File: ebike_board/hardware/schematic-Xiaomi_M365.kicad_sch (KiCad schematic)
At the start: 7 parts, among them J1 Connector_2, J3 Connector_1, U1 ESP32-S3-DevKitC

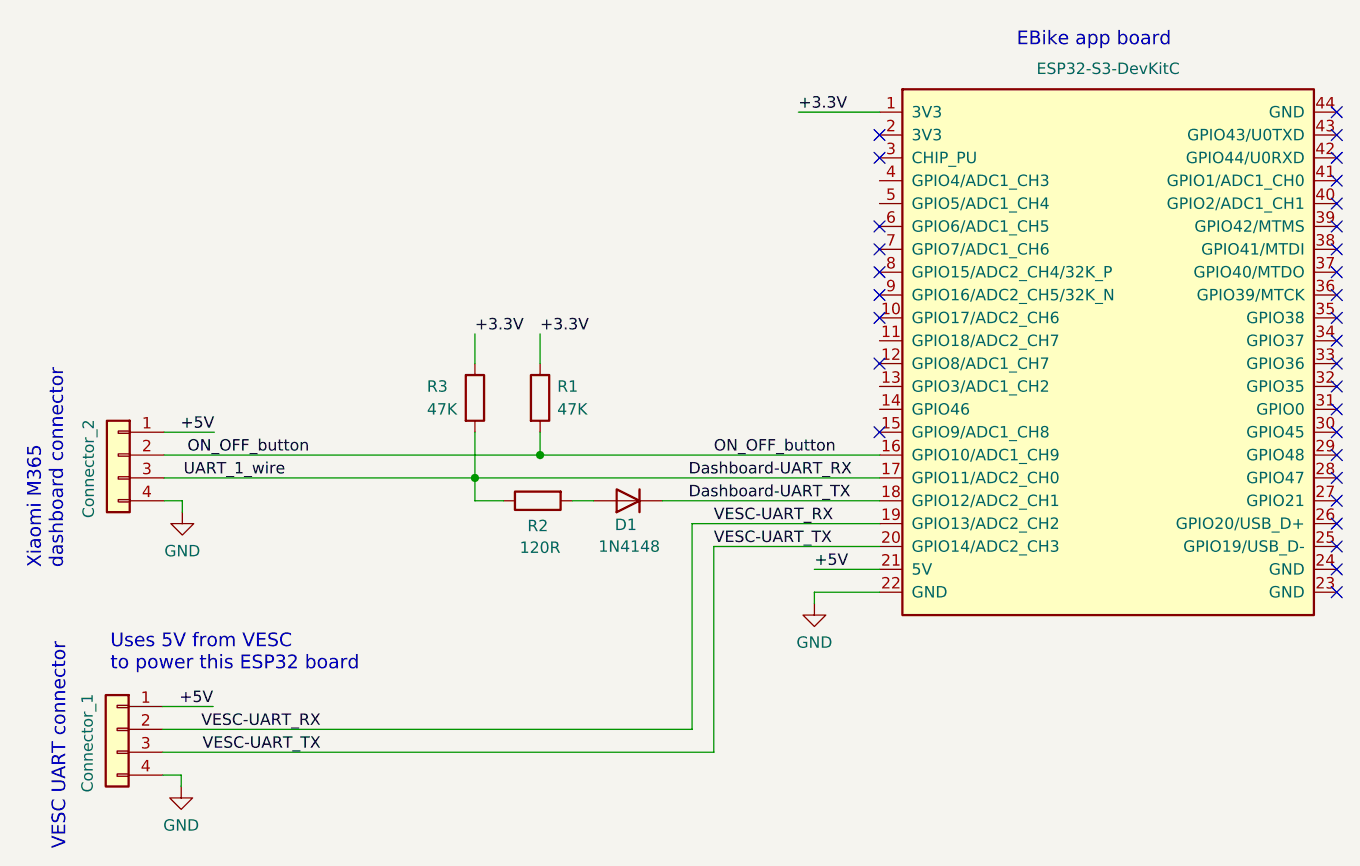
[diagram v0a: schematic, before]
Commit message: Updated schematic with tested rear light control. Rear light control works and blinks when brakes are pressed
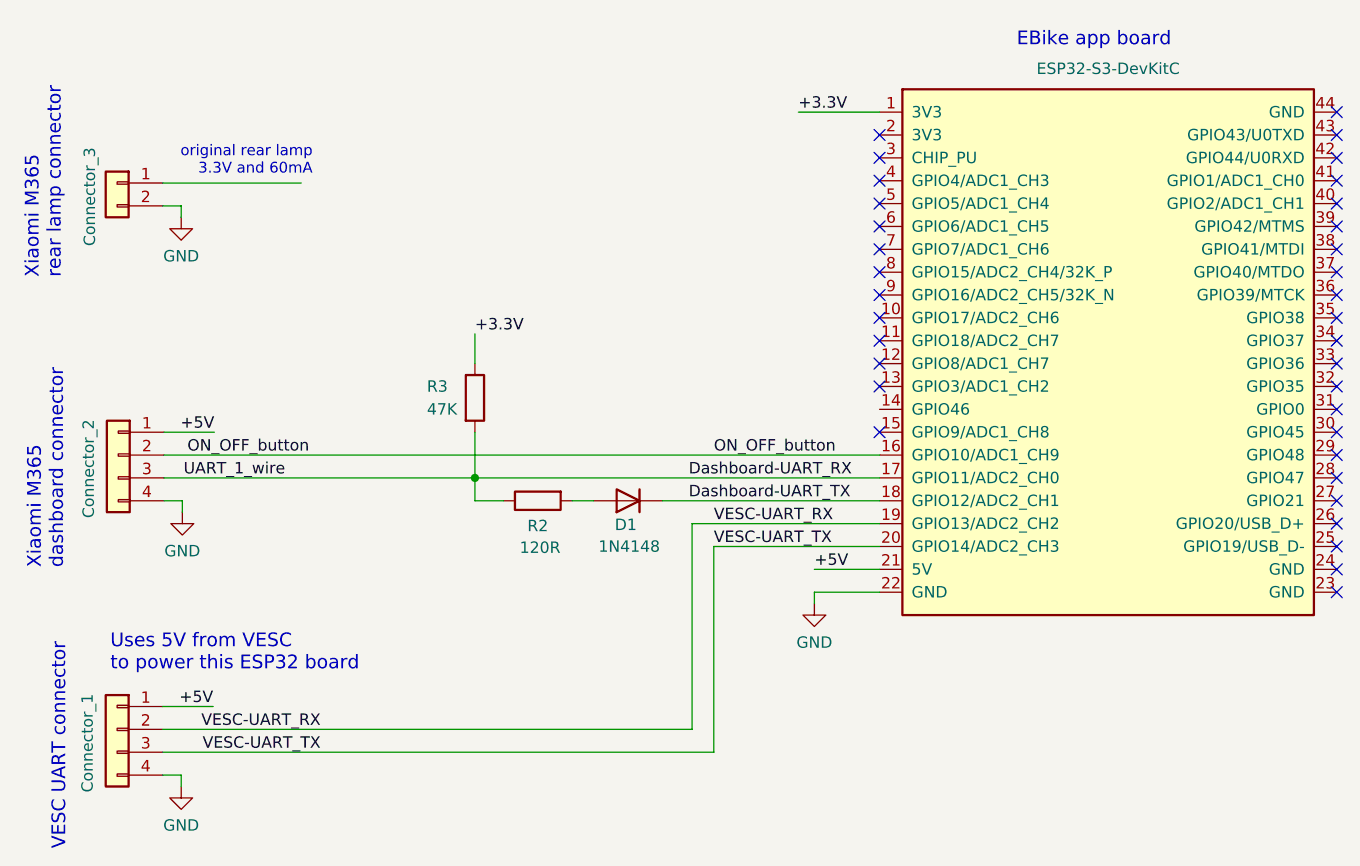
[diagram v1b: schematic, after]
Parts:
- removed R1: 47K, symbol Device:R
- added Connector_3: ~, symbol Connector_Generic:Conn_01x02
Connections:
- net GND: now also Connector_3.2 (Pin_2)
- no-connect marks 31 -> 35
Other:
- note added: "Xiaomi M365 rear lamp connector"
- note added: "original rear lamp 3.3V and 60mA"
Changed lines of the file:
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@@
   (junction (at 153.162 143.637) (diameter 0) (color 0 0 0 0)
   )
-  (junction (at 160.401 141.097) (diameter 0) (color 0 0 0 0)
-  )
+  (no_connect (at 198.12 133.477))
+  (no_connect (at 198.12 113.157))
   (no_connect (at 198.12 115.697))
   (no_connect (at 198.12 138.557))
+  (no_connect (at 198.12 128.397))
   (no_connect (at 248.92 113.157))
   (no_connect (at 198.12 105.537))
@@
   (no_connect (at 248.92 120.777))
   (no_connect (at 198.12 118.237))
-  (wire (pts (xy 160.401 130.937) (xy 160.401 127.635))
-    (stroke (width 0) (type default) (color 204 102 0 1))
-  )
+  (no_connect (at 198.12 110.617))
   (wire (pts (xy 153.162 138.557) (xy 153.162 143.637))
     (stroke (width 0) (type default))
   )
-  (wire (pts (xy 160.401 138.557) (xy 160.401 141.097))
+  (wire (pts (xy 118.491 110.871) (xy 133.858 110.871))
     (stroke (width 0) (type default))
   )
@@
   )
   (wire (pts (xy 173.99 146.177) (xy 198.12 146.177))
-    (stroke (width 0) (type default))
-  )
-  (wire (pts (xy 160.401 141.097) (xy 198.12 141.097))
     (stroke (width 0) (type default))
   )
@@
     (stroke (width 0) (type default))
   )
+  (wire (pts (xy 120.523 113.411) (xy 120.523 114.681))
+    (stroke (width 0) (type default) (color 0 0 0 1))
+  )
+  (wire (pts (xy 118.491 113.411) (xy 120.523 113.411))
+    (stroke (width 0) (type default) (color 0 0 0 1))
+  )
   (wire (pts (xy 198.12 156.337) (xy 190.881 156.337))
     (stroke (width 0) (type default) (color 0 0 0 1))
@@
     (stroke (width 0) (type default) (color 0 0 0 1))
   )
-  (wire (pts (xy 118.618 141.097) (xy 160.401 141.097))
+  (wire (pts (xy 118.618 141.097) (xy 198.12 141.097))
     (stroke (width 0) (type default))
   )
@@
     (stroke (width 0) (type default) (color 204 102 0 1))
   )
+  (text "original rear lamp\n3.3V and 60mA" (at 135.128 110.109 0)
+    (effects (font (size 1.2 1.2)) (justify right bottom))
+  )
   (text "Xiaomi M365\ndashboard connector" (at 107.569 153.797 90)
     (effects (font (size 1.524 1.524)) (justify left bottom))
@@
     (effects (font (size 1.524 1.524)) (justify left bottom))
   )
+  (text "Xiaomi M365\nrear lamp connector" (at 107.315 121.539 90)
+    (effects (font (size 1.524 1.524)) (justify left bottom))
+  )
   (text "VESC UART connector" (at 107.823 185.039 90)
     (effects (font (size 1.524 1.524)) (justify left bottom))
@@
     (effects (font (size 1.27 1.27)) (justify right bottom))
   )
-  (label "+3.3V" (at 160.401 127.635 0) (fields_autoplaced)
-    (effects (font (size 1.27 1.27)) (justify left bottom))
-  )
   (label "VESC-UART_RX" (at 179.705 148.717 0) (fields_autoplaced)
     (effects (font (size 1.27 1.27)) (justify left bottom))
+  )
+  (symbol (lib_id "Connector_Generic:Conn_01x02") (at 113.411 110.871 0) (mirror y) (unit 1)
+    (in_bom yes) (on_board yes) (dnp no)
+    (property "Reference" "Connector_3" (at 110.363 112.395 90)
+      (effects (font (size 1.27 1.27)))
+    )
+    (property "Value" "~" (at 113.411 116.205 0)
+      (effects (font (size 1.27 1.27)) hide)
+    )
+    (property "Footprint" "" (at 113.411 110.871 0)
+      (effects (font (size 1.27 1.27)) hide)
+    )
+    (property "Datasheet" "~" (at 113.411 110.871 0)
+      (effects (font (size 1.27 1.27)) hide)
+    )
+    (pin "1")
+    (pin "2")
+    (instances
+      (project "schematic-Xiaomi_M365"
+        (path "/b96fe6ac-3535-4455-ab88-ed77f5e46d6e"
+          (reference "Connector_3") (unit 1)
+        )
+      )
+    )
   )
   (symbol (lib_id "Device:R") (at 160.147 146.177 90) (mirror x) (unit 1)
@@
     )
   )
-  (symbol (lib_id "Device:R") (at 160.401 134.747 0) (unit 1)
-    (in_bom yes) (on_board yes) (dnp no)
-    (property "Reference" "R1" (at 162.306 133.477 0)
-      (effects (font (size 1.27 1.27)) (justify left))
-    )
-    (property "Value" "47K" (at 162.306 136.017 0)
-      (effects (font (size 1.27 1.27)) (justify left))
-    )
-    (property "Footprint" "" (at 158.623 134.747 90)
-      (effects (font (size 1.27 1.27)) hide)
-    )
-    (property "Datasheet" "~" (at 160.401 134.747 0)
-      (effects (font (size 1.27 1.27)) hide)
-    )
-    (pin "1")
-    (pin "2")
-    (instances
-      (project "schematic-Xiaomi_M365"
-        (path "/b96fe6ac-3535-4455-ab88-ed77f5e46d6e"
-          (reference "R1") (unit 1)
-        )
-      )
+  (symbol (lib_id "power:GND") (at 120.523 114.681 0) (unit 1)
+    (in_bom yes) (on_board yes) (dnp no)
+    (property "Reference" "#PWR02" (at 120.523 121.031 0)
+      (effects (font (size 1.27 1.27)) hide)
+    )
+    (property "Value" "GND" (at 120.523 118.999 0)
+      (effects (font (size 1.27 1.27)))
+    )
+    (property "Footprint" "" (at 120.523 114.681 0)
+      (effects (font (size 1.27 1.27)) hide)
+    )
+    (property "Datasheet" "" (at 120.523 114.681 0)
+      (effects (font (size 1.27 1.27)) hide)
+    )
+    (pin "1")
+    (instances
+      (project "schematic-Xiaomi_M365"
+        (path "/b96fe6ac-3535-4455-ab88-ed77f5e46d6e"
+          (reference "#PWR02") (unit 1)
+        )
+      )

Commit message: Little update to schematic labels. Added pictures of final instalation of Xiaomi M365
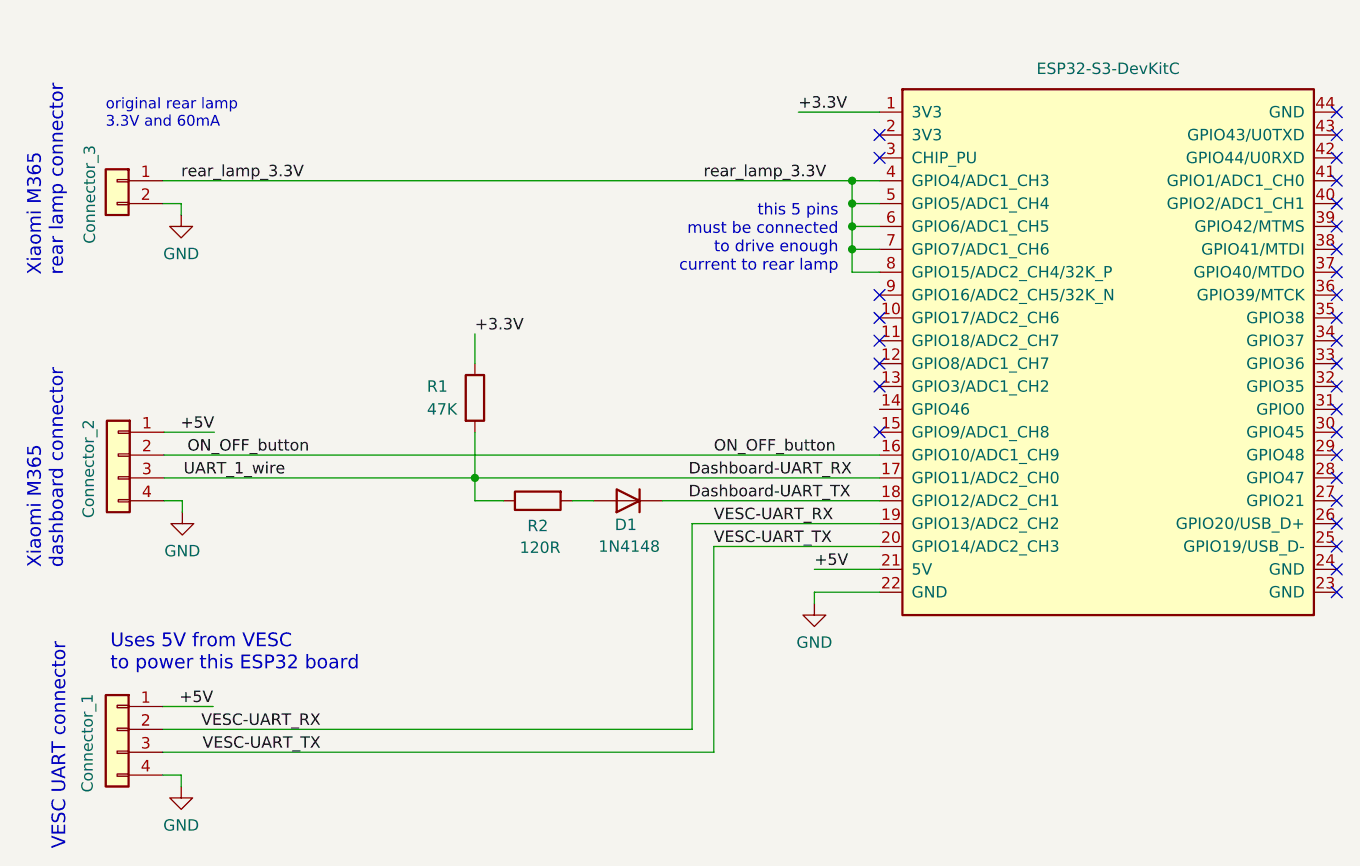
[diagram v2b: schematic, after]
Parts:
- renumbered J3 to J1, J1 to J2, R3 to R1
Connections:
- net rear_lamp_3.3V: now reaches Connector_3.1 (Pin_1)
- net rear_lamp_3.3V: now also U1.4 (GPIO4/ADC1_CH3), U1.5 (GPIO5/ADC1_CH4), U1.6 (GPIO6/ADC1_CH5), U1.7 (GPIO7/ADC1_CH6), U1.8 (GPIO15/ADC2_CH4/32K_P)
- no-connect marks 35 -> 30
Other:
- note added: "this 5 pins must be connected to drive enough current to rear lamp"
- note removed: "EBike app board"

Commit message: Added pull up resistor to the on/off button of Xiaomi M365 dashboard signal
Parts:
- added R3: 47K, symbol Device:R
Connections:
- net +3.3V: now also R3.1
- net ON_OFF_button: now also R3.2
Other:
- note added: "this 5 pins must all be connected to drive enough current to rear lamp"
- note removed: "this 5 pins must be connected to drive enough current to rear lamp"
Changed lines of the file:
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@@
   (junction (at 195.072 110.617) (diameter 0) (color 0 0 0 0)
+  )
+  (junction (at 169.926 141.097) (diameter 0) (color 0 0 0 0)
   )
   (junction (at 195.072 115.697) (diameter 0) (color 0 0 0 0)
@@
     (stroke (width 0) (type default))
   )
+  (wire (pts (xy 169.926 141.097) (xy 198.12 141.097))
+    (stroke (width 0) (type default))
+  )
   (wire (pts (xy 173.99 146.177) (xy 198.12 146.177))
     (stroke (width 0) (type default))
@@
     (stroke (width 0) (type default))
   )
+  (wire (pts (xy 169.926 130.937) (xy 169.926 127.635))
+    (stroke (width 0) (type default) (color 204 102 0 1))
+  )
   (wire (pts (xy 156.337 146.177) (xy 153.162 146.177))
+    (stroke (width 0) (type default))
+  )
+  (wire (pts (xy 169.926 138.557) (xy 169.926 141.097))
     (stroke (width 0) (type default))
   )
@@
     (stroke (width 0) (type default) (color 0 0 0 1))
   )
-  (wire (pts (xy 118.618 141.097) (xy 198.12 141.097))
+  (wire (pts (xy 118.618 141.097) (xy 169.926 141.097))
     (stroke (width 0) (type default))
   )
@@
     (effects (font (size 1.524 1.524)) (justify left bottom))
   )
-  (text "this 5 pins\nmust be connected\nto drive enough\ncurrent to rear lamp\n"
-    (at 193.548 120.904 0)
+  (text "this 5 pins\nmust all be connected\nto drive enough\ncurrent to rear lamp\n"
+    (at 193.548 120.396 0)
     (effects (font (size 1.27 1.27)) (justify right bottom))
   )
@@
   )
   (label "rear_lamp_3.3V" (at 178.562 110.617 0) (fields_autoplaced)
+    (effects (font (size 1.27 1.27)) (justify left bottom))
+  )
+  (label "+3.3V" (at 169.926 127.635 0) (fields_autoplaced)
     (effects (font (size 1.27 1.27)) (justify left bottom))
   )
@@
         )
       )
+    )
+  )
+  (symbol (lib_id "Device:R") (at 169.926 134.747 0) (unit 1)
+    (in_bom yes) (on_board yes) (dnp no)
+    (property "Reference" "R3" (at 164.592 133.477 0)
+      (effects (font (size 1.27 1.27)) (justify left))
+    )
+    (property "Value" "47K" (at 164.592 136.017 0)
+      (effects (font (size 1.27 1.27)) (justify left))
+    )
+    (property "Footprint" "" (at 168.148 134.747 90)
+      (effects (font (size 1.27 1.27)) hide)
+    )
+    (property "Datasheet" "~" (at 169.926 134.747 0)
+      (effects (font (size 1.27 1.27)) hide)
+    )
+    (pin "1")
+    (pin "2")
+    (instances
+      (project "schematic-Xiaomi_M365"
+        (path "/b96fe6ac-3535-4455-ab88-ed77f5e46d6e"
+          (reference "R3") (unit 1)
+        )
+      )
